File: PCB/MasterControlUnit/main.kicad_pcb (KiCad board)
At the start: 2 copper layers, 150.7 x 92.4 mm, 3 parts, among them U1 STM32F407G-DISC1

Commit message: Uncompleted PCB version
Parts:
- added C1: 10nF, Capacitor_THT:CP_Radial_D6.3mm_P2.50mm, F.Cu at (134.6, 54.8)
- added C2: 10nF, Capacitor_THT:CP_Radial_D6.3mm_P2.50mm, F.Cu at (130.0, 54.6)
- added FusesStatus_1: Conn_02x09_Top_Bottom, Connector_PinHeader_2.54mm:PinHeader_2x09_P2.54mm_Vertical, F.Cu at (89.5, 136.6)
- added J1: Reset Button, Connector_PinHeader_2.54mm:PinHeader_1x02_P2.54mm_Vertical, F.Cu at (264.7, 52.2)
- added J2: Start Button, Connector_PinHeader_2.54mm:PinHeader_1x02_P2.54mm_Vertical, F.Cu at (269.3, 52.2)
- added J3: An-IN, Connector_PinHeader_2.54mm:PinHeader_1x03_P2.54mm_Vertical, F.Cu at (122.2, 53.0)
- added R1: 100K, Resistor_SMD:R_1206_3216Metric, F.Cu at (265.2, 58.7)
- added R2: 4.7K, Resistor_SMD:R_1206_3216Metric, B.Cu at (183.3, 103.7)
- added R3: 4.7K, Resistor_SMD:R_1206_3216Metric, B.Cu at (183.4, 111.4)
- added R4: 12K, Resistor_SMD:R_1206_3216Metric, F.Cu at (117.1, 59.3)
- added R5: 12K, Resistor_SMD:R_1206_3216Metric, F.Cu at (119.7, 59.3)
- added R6: 1K, Resistor_SMD:R_1206_3216Metric, B.Cu at (128.6, 73.9)
- added R7: 1K, Resistor_SMD:R_1206_3216Metric, F.Cu at (133.8, 63.9)
- added R8: 22K, Resistor_SMD:R_1206_3216Metric, F.Cu at (122.2, 59.3)
- added R9: 22K, Resistor_SMD:R_1206_3216Metric, F.Cu at (126.1, 59.3)
- added U10: APS6404L-3SQR-SN, APS6404L-3SQR-SN:APS6404L-3SQR-SN_APY, F.Cu at (245.4, 123.5)
- added U11: APS6404L-3SQR-SN, APS6404L-3SQR-SN:APS6404L-3SQR-SN_APY, F.Cu at (245.4, 130.1)
- added U12: APS6404L-3SQR-SN, APS6404L-3SQR-SN:APS6404L-3SQR-SN_APY, F.Cu at (245.4, 136.8)
- added U13: 74HC138, 74HC138:SOIC127P600X175-16N, F.Cu at (253.5, 112.4)
- added U14: 74HC138, 74HC138:SOIC127P600X175-16N, F.Cu at (261.4, 112.4)
- added U15: MCP23017_SO, Package_SO:SOIC-28W_7.5x17.9mm_P1.27mm, F.Cu at (159.9, 68.5)
- added U16: ESP32-DevKitC, Espressif:ESP32-DevKitC, F.Cu at (201.7, 116.3)
- added U17: ADA4096-2ARMZ, ADA4096-2ARMZ:RM_8_ADI, F.Cu at (138.3, 69.3)
- added U2: APS6404L-3SQR-SN, APS6404L-3SQR-SN:APS6404L-3SQR-SN_APY, F.Cu at (237.0, 110.2)
- added U3: APS6404L-3SQR-SN, APS6404L-3SQR-SN:APS6404L-3SQR-SN_APY, F.Cu at (237.0, 116.8)
- added U4: APS6404L-3SQR-SN, APS6404L-3SQR-SN:APS6404L-3SQR-SN_APY, F.Cu at (237.0, 123.5)
- added U5: LD1117, Package_TO_SOT_SMD:SOT-223-3_TabPin2, F.Cu at (146.2, 55.0)
- added U6: APS6404L-3SQR-SN, APS6404L-3SQR-SN:APS6404L-3SQR-SN_APY, F.Cu at (237.0, 130.1)
- added U7: APS6404L-3SQR-SN, APS6404L-3SQR-SN:APS6404L-3SQR-SN_APY, F.Cu at (237.0, 136.8)
- added U8: APS6404L-3SQR-SN, APS6404L-3SQR-SN:APS6404L-3SQR-SN_APY, F.Cu at (245.4, 110.2)
- added U9: APS6404L-3SQR-SN, APS6404L-3SQR-SN:APS6404L-3SQR-SN_APY, F.Cu at (245.4, 116.8)
- moved DirControl_1 96.0 mm to (179.4, 52.6), turned to -90 degrees
- moved I/O-LinesToMicro_1 23.5 mm to (107.2, 53.3), turned to -90 degrees
- moved U1 13.6 mm to (118.7, 95.0), turned to -90 degrees
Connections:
- U1 pad P1_1: unconnected-(U1A-GND_P1_1-PadP1_1) -> GND
- U1 pad P1_10: unconnected-(U1A-PC2-PadP1_10) -> I/O-1 Micro
- U1 pad P1_11: unconnected-(U1A-PA1-PadP1_11) -> I/O-3 Micro
- U1 pad P1_12: unconnected-(U1A-PA0-PadP1_12) -> I/O-13 Micro
- U1 pad P1_13: unconnected-(U1A-PA3-PadP1_13) -> I/O-4 Micro
- U1 pad P1_14: unconnected-(U1A-PA2-PadP1_14) -> I/O-14 Micro
- U1 pad P1_15: unconnected-(U1A-PA5-PadP1_15) -> SCL/SCK to OSRAM
- U1 pad P1_16: unconnected-(U1A-PA4-PadP1_16) -> I/O-15 Micro
- U1 pad P1_17: unconnected-(U1A-PA7-PadP1_17) -> MOSI to OSRAM
- U1 pad P1_18: unconnected-(U1A-PA6-PadP1_18) -> MISO from OSRAM
- U1 pad P1_19: unconnected-(U1A-PC5-PadP1_19) -> I/O-5 Micro
- U1 pad P1_2: unconnected-(U1A-GND_P1_2-PadP1_2) -> GND
- U1 pad P1_20: unconnected-(U1A-PC4-PadP1_20) -> I/O-16 Micro
- U1 pad P1_21: unconnected-(U1A-PB1-PadP1_21) -> I/O-6 Micro
- U1 pad P1_25: unconnected-(U1A-PE7-PadP1_25) -> I/O-7 Micro
- U1 pad P1_27: unconnected-(U1A-PE9-PadP1_27) -> I/O-8 Micro
- U1 pad P1_29: unconnected-(U1A-PE11-PadP1_29) -> OSRAM B-EN
- U1 pad P1_31: unconnected-(U1A-PE13-PadP1_31) -> OSRAM ADDR 2
- U1 pad P1_33: unconnected-(U1A-PE15-PadP1_33) -> OSRAM ADDR 1
- U1 pad P1_35: unconnected-(U1A-PB11-PadP1_35) -> OSRAM ADDR 0
- U1 pad P1_37: unconnected-(U1A-PB13-PadP1_37) -> SCL/SCK
- U1 pad P1_38: unconnected-(U1A-PB14-PadP1_38) -> MISO
- U1 pad P1_39: unconnected-(U1A-PB15-PadP1_39) -> MOSI
- U1 pad P1_41: unconnected-(U1A-PD9-PadP1_41) -> CS
- U1 pad P1_42: unconnected-(U1A-PD10-PadP1_42) -> Net-(U15-A0)
- U1 pad P1_43: unconnected-(U1A-PD11-PadP1_43) -> I/O-9 Micro
- U1 pad P1_44: unconnected-(U1A-PD12-PadP1_44) -> Net-(U15-A1)
- U1 pad P1_45: unconnected-(U1A-PD13-PadP1_45) -> I/O-10 Micro
- U1 pad P1_46: unconnected-(U1A-PD14-PadP1_46) -> Net-(U15-A2)
- U1 pad P1_47: unconnected-(U1A-PD15-PadP1_47) -> I/O-11 Micro
- U1 pad P1_50: unconnected-(U1A-GND_P1_50-PadP1_50) -> I/O-12 Micro
- U1 pad P1_6: unconnected-(U1A-~{RST}-PadP1_6) -> MCU_reset
- U1 pad P1_7: unconnected-(U1A-PC1-PadP1_7) -> Net-(U1A-PC1)
- U1 pad P1_8: unconnected-(U1A-PC0-PadP1_8) -> Net-(U1A-PC0)
- U1 pad P1_9: unconnected-(U1A-PC3-PadP1_9) -> I/O-2 Micro
- U1 pad P2_1: (no net) -> GND
- U1 pad P2_10: (no net) -> P4_CHK
- U1 pad P2_11: (no net) -> unconnected-(U1B-PE6-PadP2_11)
- U1 pad P2_12: (no net) -> P5_CHK
- U1 pad P2_13: (no net) -> unconnected-(U1B-PE4-PadP2_13)
- U1 pad P2_14: (no net) -> P6_CHK
- U1 pad P2_15: (no net) -> unconnected-(U1B-PE2-PadP2_15)
- U1 pad P2_16: (no net) -> P7_CHK
- U1 pad P2_17: (no net) -> unconnected-(U1B-PE0-PadP2_17)
- U1 pad P2_18: (no net) -> P8_CHK
- U1 pad P2_19: (no net) -> unconnected-(U1B-PB8-PadP2_19)
- U1 pad P2_2: (no net) -> GND
- U1 pad P2_20: (no net) -> PWM_2
- U1 pad P2_21: (no net) -> unconnected-(U1B-BOOT0-PadP2_21)
- U1 pad P2_22: (no net) -> P10_CHK
- U1 pad P2_23: (no net) -> I2C1_SCL ESP32
- U1 pad P2_24: (no net) -> I2C1_SDA ESP32
- U1 pad P2_25: (no net) -> MISO from ISRAM
- U1 pad P2_26: (no net) -> MOSI to ISRAM
- U1 pad P2_27: (no net) -> unconnected-(U1B-PD7-PadP2_27)
- U1 pad P2_28: (no net) -> SCL/SCK to ISRAM
- U1 pad P2_29: (no net) -> unconnected-(U1B-PD5-PadP2_29)
- U1 pad P2_3: (no net) -> +5V
- U1 pad P2_30: (no net) -> ISRAM ADDR 0
- U1 pad P2_31: (no net) -> unconnected-(U1B-PD3-PadP2_31)
- U1 pad P2_32: (no net) -> OSRAM B-EN
- U1 pad P2_33: (no net) -> unconnected-(U1B-PD1-PadP2_33)
- U1 pad P2_34: (no net) -> P11_CHK
- U1 pad P2_35: (no net) -> unconnected-(U1B-PC12-PadP2_35)
- U1 pad P2_36: (no net) -> P12_CHK
- U1 pad P2_37: (no net) -> unconnected-(U1B-PC10-PadP2_37)
- U1 pad P2_38: (no net) -> P13_CHK
- U1 pad P2_39: (no net) -> unconnected-(U1B-PA14-PadP2_39)
- U1 pad P2_4: (no net) -> P1_CHK
- U1 pad P2_40: (no net) -> P14_CHK
- U1 pad P2_41: (no net) -> unconnected-(U1B-PA10-PadP2_41)
- U1 pad P2_42: (no net) -> P15_CHK
- U1 pad P2_43: (no net) -> unconnected-(U1B-PA8-PadP2_43)
- U1 pad P2_44: (no net) -> P16_CHK
- U1 pad P2_45: (no net) -> PWM_1
- U1 pad P2_46: (no net) -> P3_CHK
- U1 pad P2_47: (no net) -> unconnected-(U1B-PC6-PadP2_47)
- U1 pad P2_48: (no net) -> P9_CHK
- U1 pad P2_49: (no net) -> unconnected-(U1B-GND_P2_49-PadP2_49)
- U1 pad P2_5: (no net) -> unconnected-(U1B-3V_P2_5-PadP2_5)
- U1 pad P2_50: (no net) -> unconnected-(U1B-GND_P2_50-PadP2_50)
- U1 pad P2_6: (no net) -> P2_CHK
- U1 pad P2_7: (no net) -> unconnected-(U1B-PH0-PadP2_7)
- U1 pad P2_8: (no net) -> unconnected-(U1B-PH1-PadP2_8)
- U1 pad P2_9: (no net) -> unconnected-(U1B-PC14-PadP2_9)
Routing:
- net GND: track 0.00 -> 201.8 mm, vias 0 -> 3
- net Net-(U15-A2): track 0.00 -> 97.9 mm, vias 0 -> 2
- net Net-(U15-A0): track 0.00 -> 97.0 mm, vias 0 -> 2
- net Net-(U15-A1): track 0.00 -> 96.0 mm, vias 0 -> 2
- net I/O-13 Micro: track 0.00 -> 93.1 mm, vias 0 -> 1
- net +5V: track 0.00 -> 89.6 mm, vias 0 -> 2
- net I/O-15 Micro: track 0.00 -> 84.0 mm, vias 0 -> 3
- net I/O-14 Micro: track 0.00 -> 75.4 mm
- net I/O-16 Micro: track 0.00 -> 74.1 mm, vias 0 -> 1
- net +3.3V: track 0.00 -> 73.3 mm, vias 0 -> 2
- net Net-(U17-INA+): track 0.00 -> 71.0 mm
- net I/O-1 Micro: track 0.00 -> 67.2 mm
- net DIR-4: track 0.00 -> 63.0 mm, vias 0 -> 2
- net P6_CHK: track 0.00 -> 60.6 mm, vias 0 -> 3
- net P4_CHK: track 0.00 -> 58.6 mm, vias 0 -> 3
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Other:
- board text added: "GPIO22"

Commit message: Multilayer version
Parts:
- R2, R3: moved to F.Cu
- R7: moved to B.Cu
- U5: value LD1117 -> LD1117S33TR_SOT223
- moved U14 145.1 mm to (117.3, 95.7), turned to 180 degrees
- moved U10 143.8 mm to (109.1, 169.2)
- moved U11 143.8 mm to (109.1, 175.9)
- moved U12 143.8 mm to (109.1, 182.5)
- moved U2 143.8 mm to (100.7, 155.9)
- moved U3 143.8 mm to (100.7, 162.6)
- moved U4 143.8 mm to (100.7, 169.2)
- moved U6 143.8 mm to (100.7, 175.9)
- moved U7 143.8 mm to (100.7, 182.5)
- moved U8 143.8 mm to (109.1, 155.9)
- moved U9 143.8 mm to (109.1, 162.6)
- moved U13 123.9 mm to (148.0, 177.3)
- moved DirControl_1 107.7 mm to (112.3, 136.8), turned to 90 degrees
- moved U5 91.7 mm to (103.7, 136.2), turned to -90 degrees
- moved J1 73.5 mm to (214.3, 105.7), turned to 180 degrees
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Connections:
- U1 pad P1_36: unconnected-(U1A-PB12-PadP1_36) -> ISRAM ADDR 0
- U1 pad P1_37: SCL/SCK -> SCL/SCK to ISRAM
- U1 pad P1_38: MISO -> MISO from ISRAM
- U1 pad P1_39: MOSI -> MOSI to ISRAM
- U1 pad P1_41: CS -> ISRAM B-EN
- U1 pad P2_32: OSRAM B-EN -> ISRAM B-EN
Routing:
- net GND: track 201.8 -> 568.1 mm, vias 3 -> 6
- net +5V: track 89.6 -> 355.2 mm, vias 2 -> 3
- net OSRAM ADDR 2: track 0.00 -> 120.1 mm
- net ISRAM ADDR 0: track 0.00 -> 108.1 mm, vias 0 -> 1
- net OSRAM ADDR 1: track 0.00 -> 102.0 mm
- net OSRAM ADDR 0: track 0.00 -> 100.6 mm
- net I2C1_SCL ESP32: track 5.66 -> 104.0 mm, vias 0 -> 2
- net I2C1_SDA ESP32: track 5.55 -> 100.3 mm, vias 0 -> 3
- net OSRAM B-EN: track 0.00 -> 81.1 mm
- net SCL/SCK to ISRAM: track 0.00 -> 75.2 mm
- net +3.3V: track 73.3 -> 144.7 mm, vias 2 -> 6
- net Net-(J3-Pin_2): track 4.80 -> 71.0 mm
- net Net-(J3-Pin_3): track 4.80 -> 67.9 mm
- net P1_CHK: track 57.7 -> 118.0 mm, vias 1 -> 0
- net MCU_reset: track 44.8 -> 104.2 mm
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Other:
- copper layers 2 -> 4
- board text removed: "GPIO22"

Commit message: First completed version
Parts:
- moved U13 112.7 mm to (110.7, 71.0), turned to -90 degrees
- moved U7 101.9 mm to (122.5, 83.0), turned to -90 degrees
- moved U12 101.5 mm to (128.6, 82.9), turned to -90 degrees
- moved U10 98.7 mm to (120.1, 71.1), turned to -90 degrees
- moved U11 93.2 mm to (116.3, 83.0), turned to -90 degrees
- moved U6 93.0 mm to (103.7, 82.9), turned to -90 degrees
- moved U9 91.8 mm to (101.8, 71.1), turned to -90 degrees
- moved U3 88.7 mm to (168.4, 105.3)
- moved U4 86.8 mm to (110.1, 83.0), turned to -90 degrees
- moved U2 80.8 mm to (168.3, 111.6)
- moved U8 74.0 mm to (97.2, 82.9), turned to -90 degrees
- moved U14 42.7 mm to (158.3, 107.6), turned to 0 degrees
- moved R6 1.29 mm to (95.8, 73.4)
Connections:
- U1 pad P1_36: ISRAM ADDR 0 -> unconnected-(U1A-PB12-PadP1_36)
- U1 pad P1_37: SCL/SCK to ISRAM -> SCL/SCK
- U1 pad P1_38: MISO from ISRAM -> MISO
- U1 pad P1_39: MOSI to ISRAM -> MOSI
- U1 pad P1_41: ISRAM B-EN -> CS
- U7 pad 8: unconnected-(U7-VDD-Pad8) -> +3.3V
- U9 pad 2: unconnected-(U9-SO/SIO[1]-Pad2) -> MOSI to OSRAM
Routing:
- net MISO from OSRAM: track 0.00 -> 224.5 mm, vias 0 -> 2
- net MOSI to OSRAM: track 0.00 -> 221.0 mm, vias 0 -> 2
- net SCL/SCK to OSRAM: track 0.00 -> 199.6 mm, vias 0 -> 3
- net OSRAM B-EN: track 81.1 -> 232.6 mm
- net GND: track 568.1 -> 673.4 mm, vias 6 -> 9
- net +3.3V: track 144.7 -> 234.1 mm, vias 6 -> 17
- net ISRAM B-EN: track 0.00 -> 84.4 mm, vias 0 -> 1
- net MCU_reset: track 104.2 -> 185.3 mm, vias 2 -> 3
- net MOSI to ISRAM: track 0.00 -> 68.3 mm
- net Net-(U11-/CE): track 0.00 -> 34.9 mm, vias 0 -> 2
- net OSRAM ADDR 1: track 102.0 -> 134.1 mm, vias 0 -> 2
- net Net-(U10-/CE): track 0.00 -> 29.2 mm, vias 0 -> 1
- net Net-(U12-/CE): track 0.00 -> 28.7 mm, vias 0 -> 2
- net SCL/SCK to ISRAM: track 75.2 -> 99.0 mm
- net OSRAM ADDR 2: track 120.1 -> 143.3 mm, vias 0 -> 2
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
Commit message: Fixes
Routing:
- net DIR-5: track 0.00 -> 36.5 mm, vias 0 -> 1
- net GND: track 673.4 -> 682.3 mm, vias 9 -> 11
- net I2C1_SCL ESP32: track 104.0 -> 105.4 mm
- net DIR-7: track 33.9 -> 34.5 mm
- net Net-(U13-~{Y4}): vias 1 -> 0
- net Net-(U10-/CE): vias 1 -> 0
- net +5V: vias 3 -> 2

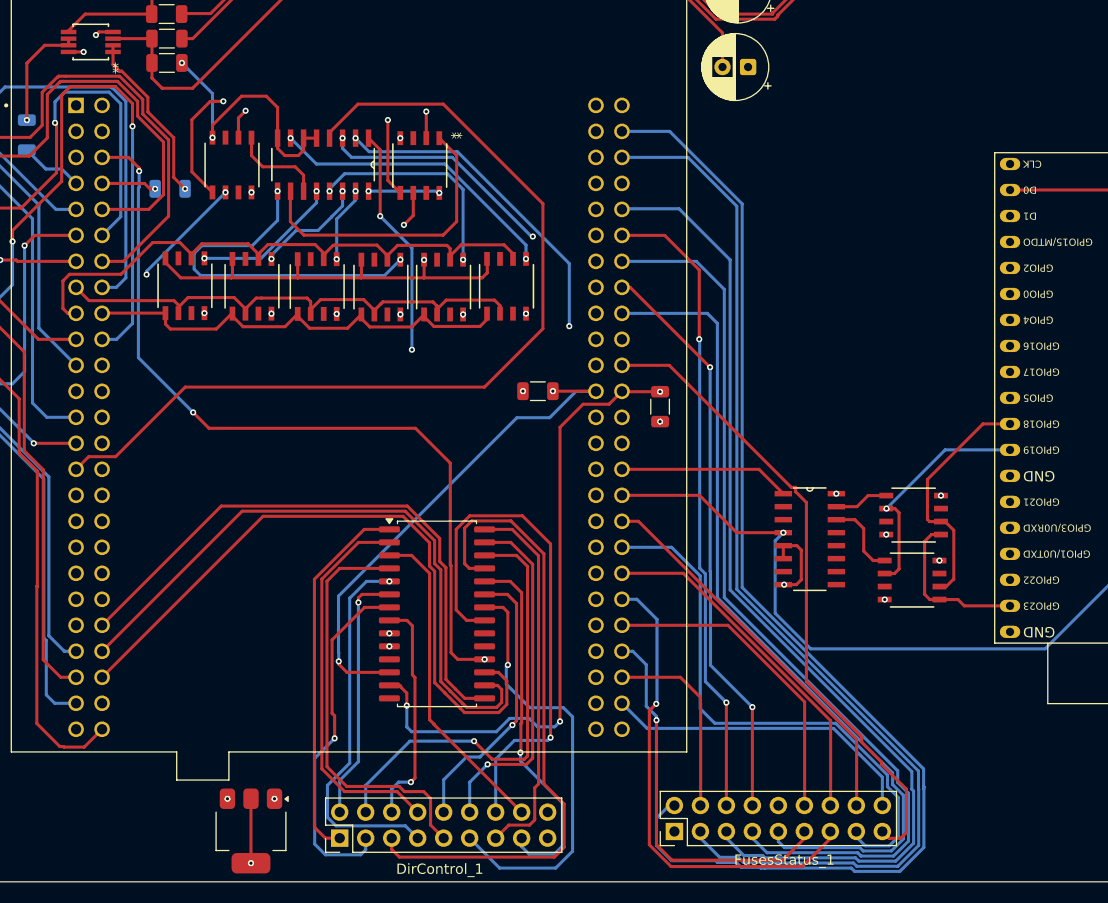
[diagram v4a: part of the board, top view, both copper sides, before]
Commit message: Add PSRAM decoupling capacitors, improve grounding and refine PCB routing
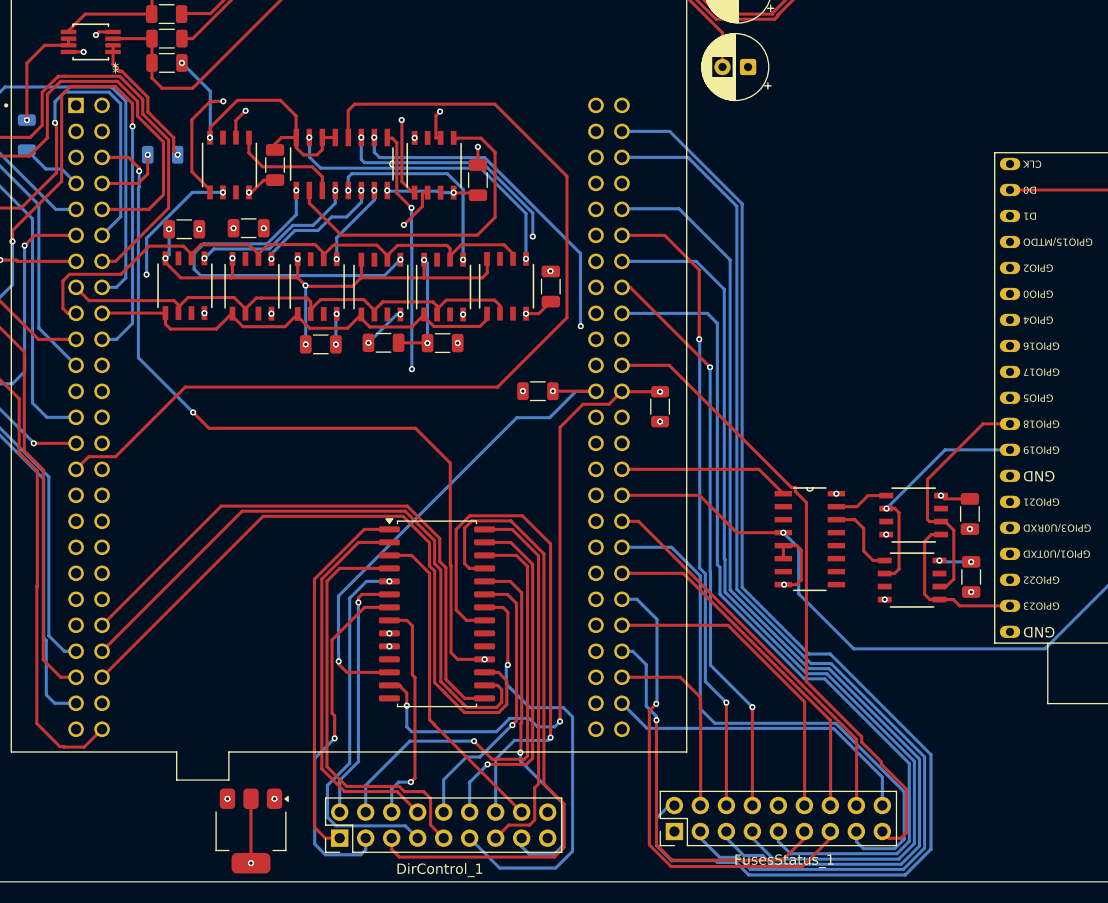
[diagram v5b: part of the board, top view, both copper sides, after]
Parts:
- added C10: 100nF, Capacitor_SMD:C_1206_3216Metric, F.Cu at (106.0, 71.1)
- added C11: 100nF, Capacitor_SMD:C_1206_3216Metric, F.Cu at (125.8, 72.5)
- added C12: 100nF, Capacitor_SMD:C_1206_3216Metric, F.Cu at (110.5, 88.6)
- added C3: 100nF, Capacitor_SMD:C_1206_3216Metric, F.Cu at (122.4, 88.5)
- added C4: 100nF, Capacitor_SMD:C_1206_3216Metric, F.Cu at (174.0, 111.3)
- added C5: 100nF, Capacitor_SMD:C_1206_3216Metric, F.Cu at (173.9, 105.2)
- added C6: 100nF, Capacitor_SMD:C_1206_3216Metric, F.Cu at (97.1, 77.3)
- added C7: 100nF, Capacitor_SMD:C_1206_3216Metric, F.Cu at (103.4, 77.2)
- added C8: 100nF, Capacitor_SMD:C_1206_3216Metric, F.Cu at (116.6, 88.5)
- added C9: 100nF, Capacitor_SMD:C_1206_3216Metric, F.Cu at (132.9, 83.0)
- moved R6 3.40 mm to (95.0, 70.1)
- moved U13 1.83 mm to (112.5, 71.0)
- moved U10 1.41 mm to (121.5, 71.1)
- moved U9 0.25 mm to (101.5, 71.1)
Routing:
- net +3.3V: track 233.8 -> 269.7 mm, vias 17 -> 23
- net GND: track 682.3 -> 716.9 mm, vias 11 -> 23
- net OSRAM B-EN: track 232.6 -> 237.6 mm
- net Net-(U17-INA-): track 17.1 -> 13.4 mm
- net Net-(U10-/CE): track 29.2 -> 32.4 mm
- net ISRAM B-EN: track 84.4 -> 81.3 mm
- net P1_CHK: track 118.0 -> 120.6 mm
- net SCL/SCK to OSRAM: track 199.6 -> 202.1 mm
- net P4_CHK: track 97.7 -> 100.1 mm
- net P2_CHK: track 107.0 -> 109.4 mm
- net P6_CHK: track 89.7 -> 92.1 mm
- net P8_CHK: track 81.7 -> 84.0 mm
- net Net-(U13-~{Y3}): track 14.3 -> 16.3 mm
- net Net-(U13-~{Y4}): track 9.20 -> 11.0 mm
- net Net-(U13-~{Y1}): track 10.8 -> 12.5 mm
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- added copper zone on In1.Cu, net GND

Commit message: Finalize HILO PCB routing and power distribution
Increase 3.3V and 5V trace widths to 0.5 mm.
Improve connector clearances and mechanical placement.
Verify ground plane continuity and PCB design rules.
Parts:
- added C13: 10uF, Capacitor_THT:C_Radial_D5.0mm_H7.0mm_P2.00mm, F.Cu at (105.3, 135.0)
- added C14: 10uF, Capacitor_THT:C_Radial_D5.0mm_H7.0mm_P2.00mm, F.Cu at (92.2, 133.3)
- moved U5 4.83 mm to (98.8, 136.2)
- moved FusesStatus_1 4.79 mm to (149.8, 136.8)
- moved DirControl_1 3.08 mm to (115.4, 136.8)
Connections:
- U5 pad 2: +5V -> +3.3V
- U5 pad 3: +3.3V -> +5V
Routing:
- net GND: track 716.9 -> 764.0 mm, vias 23 -> 24
- net +3.3V: track 269.7 -> 284.4 mm, vias 23 -> 24
- net DIR-16: track 36.9 -> 47.8 mm
- net DIR-12: track 36.0 -> 41.6 mm
- net P9_CHK: track 31.2 -> 36.5 mm
- net P11_CHK: track 38.2 -> 43.3 mm
- net P12_CHK: track 56.0 -> 51.4 mm, vias 0 -> 1
- net DIR-13: track 63.1 -> 67.6 mm
- net DIR-3: track 31.7 -> 36.1 mm
- net +5V: track 355.2 -> 351.7 mm, vias 2 -> 5
- net P13_CHK: track 34.7 -> 38.2 mm
- net OSRAM ADDR 0: track 124.5 -> 128.0 mm
- net P15_CHK: track 31.1 -> 34.6 mm
- net P4_CHK: track 100.1 -> 103.3 mm
- net P2_CHK: track 109.4 -> 112.5 mm
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- added copper zone on F.Cu, net +3.3V
